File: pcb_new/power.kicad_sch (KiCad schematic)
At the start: 36 parts, among them J2 632723300011, J3 SACC-DSIV-M12MS-5CON-L180, U11 TPS2023DR, U12 LM1085ISX-3.3/NOPB, U13 INA226AIDGSR

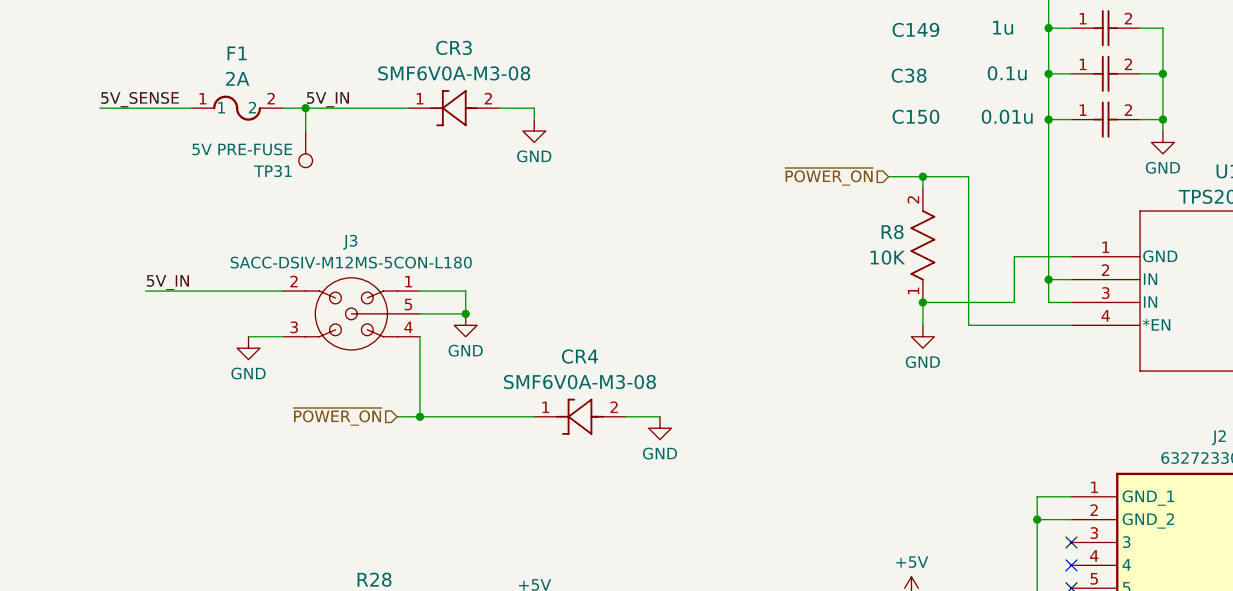
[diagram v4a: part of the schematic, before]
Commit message: separate VBUS/PSU control lines (ref #89) and pull up VBUS enable (ref #68)
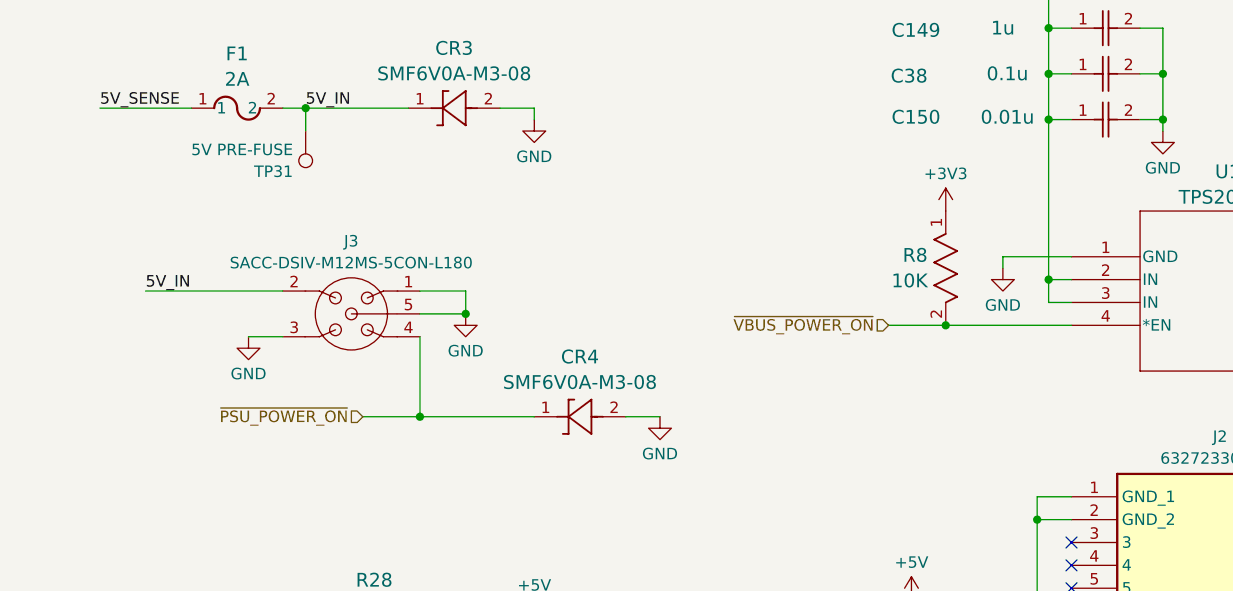
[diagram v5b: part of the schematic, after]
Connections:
- net +3V3: now also R8.1
- net GND: no longer R8.1
- net ~{POWER_ON} renamed ~{PSU_POWER_ON}
- net ~{PSU_POWER_ON}: no longer R8.2, U11.4 (*EN)
- new net ~{VBUS_POWER_ON}: R8.2, U11.4 (*EN)
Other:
- moved on the sheet: R8
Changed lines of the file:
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@@
 	)
 	(junction
-		(at 190.5 57.15)
+		(at 107.95 163.83)
 		(diameter 0)
 		(color 0 0 0 0)
 	)
 	(junction
-		(at 107.95 163.83)
+		(at 193.04 59.69)
 		(diameter 0)
 		(color 0 0 0 0)
@@
 	)
 	(junction
-		(at 190.5 43.18)
-		(diameter 0)
-		(color 0 0 0 0)
-	)
-	(junction
 		(at 129.54 124.46)
 		(diameter 0)
@@
 	(wire
 		(pts
-			(xy 132.08 69.85) (xy 134.62 69.85)
+			(xy 128.27 69.85) (xy 134.62 69.85)
 		)
 		(stroke
@@
 	(wire
 		(pts
-			(xy 195.58 59.69) (xy 207.01 59.69)
-		)
-		(stroke
-			(width 0)
-			(type default)
-		)
-	)
-	(wire
-		(pts
 			(xy 129.54 124.46) (xy 130.81 124.46)
 		)
@@
 	(wire
 		(pts
-			(xy 186.69 43.18) (xy 190.5 43.18)
+			(xy 186.69 59.69) (xy 193.04 59.69)
 		)
 		(stroke
@@
 	(wire
 		(pts
-			(xy 107.95 158.75) (xy 107.95 163.83)
+			(xy 193.04 59.69) (xy 207.01 59.69)
 		)
 		(stroke
@@
 	(wire
 		(pts
-			(xy 49.53 173.99) (xy 49.53 176.53)
+			(xy 107.95 158.75) (xy 107.95 163.83)
 		)
 		(stroke
@@
 	(wire
 		(pts
-			(xy 104.14 111.76) (xy 115.57 111.76)
+			(xy 49.53 173.99) (xy 49.53 176.53)
 		)
 		(stroke
@@
 	(wire
 		(pts
-			(xy 38.1 114.3) (xy 43.18 114.3)
+			(xy 104.14 111.76) (xy 115.57 111.76)
 		)
 		(stroke
@@
 	(wire
 		(pts
-			(xy 195.58 43.18) (xy 195.58 59.69)
+			(xy 38.1 114.3) (xy 43.18 114.3)
 		)
 		(stroke
@@
 	(wire
 		(pts
-			(xy 200.66 57.15) (xy 190.5 57.15)
-		)
-		(stroke
-			(width 0)
-			(type default)
-		)
-	)
-	(wire
-		(pts
 			(xy 129.54 119.38) (xy 129.54 124.46)
 		)
@@
 	(wire
 		(pts
-			(xy 190.5 44.45) (xy 190.5 43.18)
-		)
-		(stroke
-			(width 0)
-			(type default)
-		)
-	)
-	(wire
-		(pts
 			(xy 256.54 27.94) (xy 255.27 27.94)
 		)
@@
 	(wire
 		(pts
-			(xy 190.5 59.69) (xy 190.5 57.15)
-		)
-		(stroke
-			(width 0)
-			(type default)
-		)
-	)
-	(wire
-		(pts
 			(xy 246.38 52.07) (xy 259.08 52.07)
 		)
@@
 	(wire
 		(pts
-			(xy 190.5 43.18) (xy 195.58 43.18)
-		)
-		(stroke
-			(width 0)
-			(type default)
-		)
-	)
-	(wire
-		(pts
 			(xy 204.47 36.83) (xy 204.47 54.61)
 		)
@@
 	(wire
 		(pts
-			(xy 207.01 52.07) (xy 200.66 52.07)
+			(xy 207.01 52.07) (xy 199.39 52.07)
 		)
 		(stroke
@@
 	(wire
 		(pts
-			(xy 200.66 52.07) (xy 200.66 57.15)
+			(xy 255.27 143.51) (xy 243.84 143.51)
 		)
 		(stroke
@@
 	(wire
 		(pts
-			(xy 255.27 143.51) (xy 243.84 143.51)
+			(xy 214.63 31.75) (xy 217.17 31.75)
 		)
 		(stroke
@@
 	(wire
 		(pts
-			(xy 214.63 31.75) (xy 217.17 31.75)
+			(xy 243.84 140.97) (xy 255.27 140.97)
 		)
 		(stroke
@@
 	(wire
 		(pts
-			(xy 243.84 140.97) (xy 255.27 140.97)
+			(xy 199.39 52.07) (xy 199.39 53.34)
 		)
 		(stroke
@@
 		)
 	)
-	(hierarchical_label "~{POWER_ON}"
+	(hierarchical_label "~{PSU_POWER_ON}"
 		(shape input)
-		(at 132.08 69.85 180)
+		(at 128.27 69.85 180)
 		(fields_autoplaced yes)
 		(effects
@@
 		)
 	)
-	(hierarchical_label "~{POWER_ON}"
+	(hierarchical_label "~{VBUS_POWER_ON}"
 		(shape input)
-		(at 186.69 43.18 180)
+		(at 186.69 59.69 180)
 		(fields_autoplaced yes)
 		(effects
@@
 	)
 	(symbol
+		(lib_id "power:+3V3")
+		(at 193.04 46.99 0)
+		(unit 1)
+		(exclude_from_sim no)
+		(in_bom yes)
+		(on_board yes)
+		(dnp no)
+		(fields_autoplaced yes)
+		(property "Reference" "#PWR0198"
+			(at 193.04 50.8 0)
+			(effects
+				(font
+					(size 1.27 1.27)
+				)
+				(hide yes)
+			)
+		)
+		(property "Value" "+3V3"
+			(at 193.04 42.8569 0)
+			(effects
+				(font
+					(size 1.27 1.27)
+				)
+			)
+		)
+		(property "Footprint" ""
+			(at 193.04 46.99 0)
+			(effects
+				(font
+					(size 1.27 1.27)
+				)
+				(hide yes)
+			)
+		)
+		(property "Datasheet" ""
+			(at 193.04 46.99 0)
+			(effects
+				(font
+					(size 1.27 1.27)
+				)
+				(hide yes)
+			)
+		)
+		(property "Description" "Power symbol creates a global label with name \"+3V3\""
+			(at 193.04 46.99 0)
+			(effects
+				(font
+					(size 1.27 1.27)
+				)
+				(hide yes)
+			)
+		)
+		(pin "1"
+		)
+		(instances
+			(project "link"
+				(path "/b8dafc19-6de0-4c8f-9903-23372e5103df/efe900f0-e311-40d9-a69c-d0ffa18ab615"
+					(reference "#PWR0198")
+					(unit 1)
+				)
+			)
+		)
+	)
+	(symbol
 		(lib_id "OroLink:RMCF0402FT10K0")
 		(at 265.43 45.72 90)
@@
 	(symbol
 		(lib_id "OroLink:RMCF0402FT10K0")
-		(at 190.5 57.15 90)
+		(at 193.04 46.99 90)
+		(mirror x)
 		(unit 1)
 		(exclude_from_sim no)
@@
 		(on_board yes)
 		(dnp no)
-		(fields_autoplaced yes)
 		(property "Reference" "R8"
-			(at 188.4934 49.3835 90)
+			(at 191.0334 51.9235 90)
 			(effects
 				(font
@@
 		)
 		(property "Value" "10K"
-			(at 188.4934 52.2164 90)
+			(at 191.0334 54.7564 90)
 			(effects
 				(font
@@
 		)
 		(property "Footprint" "OroLink:STA_RMCF0402_STP"
-			(at 190.5 57.15 0)
+			(at 193.04 46.99 0)
 			(effects
 				(font
@@
 		)
 		(property "Datasheet" "https://www.mouser.de/datasheet/2/385/SEI_RMCF_RMCP-3077565.pdf"
-			(at 190.5 57.15 0)
+			(at 193.04 46.99 0)
 			(effects
 				(font
@@
 		)
 		(property "Description" "Res Thick Film 0402 10K Ohm 1% 0.063W ±100ppm/°C Molded SMD Paper T/R"
-			(at 190.5 57.15 0)
+			(at 193.04 46.99 0)
 			(effects
 				(font
@@
 		)
 		(property "Description_1" "Res Thick Film 0402 10K Ohm 1% 0.063W ±100ppm/°C Molded SMD Paper T/R"
-			(at 193.5 57.15 0)
+			(at 196.04 46.99 0)
 			(effects
 				(font
@@
 		)
 		(property "Mfr. Name" "Stackpole International"
-			(at 193.5 57.15 0)
+			(at 196.04 46.99 0)
 			(effects
 				(font
@@
 		)
 		(property "DigiKey ID" "RMCF0402FT10K0CT-ND"
-			(at 193.5 57.15 0)
+			(at 196.04 46.99 0)
 			(effects
 				(font
@@
 		)
 		(property "Mouser URL" "https://www.mouser.de/ProductDetail/SEI-Stackpole/RMCF0402FT10K0?qs=FESYatJ8odLDpjm%252BwxiA1Q%3D%3D&utm_source=octopart&utm_medium=aggregator&utm_campaign=708-RMCF0402FT10K0&utm_content=SEI%20Stackpole"
-			(at 193.5 57.15 0)
+			(at 196.04 46.99 0)
 			(effects
 				(font
@@
 		)
 		(property "Arrow ID" "RMCF0402FT10K0"
-			(at 193.5 57.15 0)
+			(at 196.04 46.99 0)
 			(effects
 				(font
@@
 		)
 		(property "Mfr. Number" "RMCF0402FT10K0"
-			(at 193.5 57.15 0)
+			(at 196.04 46.99 0)
 			(effects
 				(font
@@
 		)
 		(property "Mouser ID" "708-RMCF0402FT10K0"
-			(at 193.5 57.15 0)
+			(at 196.04 46.99 0)
 			(effects
 				(font
@@
 	(symbol
 		(lib_id "power:GND")
-		(at 190.5 59.69 0)
+		(at 199.39 53.34 0)
 		(unit 1)
 		(exclude_from_sim no)
@@
 		(dnp no)
 		(property "Reference" "#PWR020"
-			(at 190.5 66.04 0)
+			(at 199.39 59.69 0)
 			(effects
 				(font
@@
 		)
 		(property "Value" "GND"
-			(at 190.5 63.8231 0)
+			(at 199.39 57.4731 0)
 			(effects
 				(font
@@
 		)
 		(property "Footprint" ""
-			(at 190.5 59.69 0)
+			(at 199.39 53.34 0)
 			(effects
 				(font
@@
 		)
 		(property "Datasheet" ""
-			(at 190.5 59.69 0)
+			(at 199.39 53.34 0)
 			(effects
 				(font
@@
 		)
 		(property "Description" "Power symbol creates a global label with name \"GND\" , ground"
-			(at 190.5 59.69 0)
+			(at 199.39 53.34 0)
 			(effects
 				(font

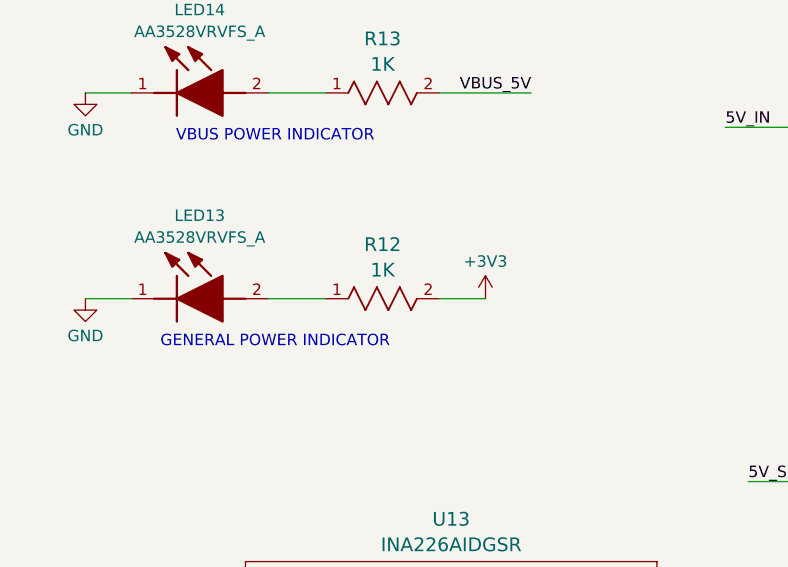
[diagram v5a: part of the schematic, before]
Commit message: reduce general power indicator light intensity
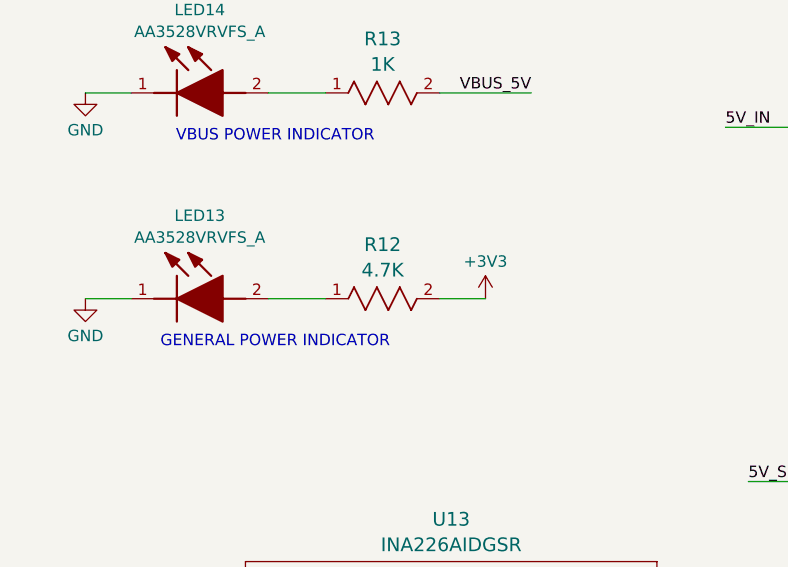
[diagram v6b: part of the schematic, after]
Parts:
- removed R12: 1K, OroLink:RES_SG73P_2A_KOA, symbol OroLink:SG73P2ATTD102J
- added R12: 4.7K, OroLink:RES_CRCW_0402_VIS-L, symbol OroLink:CRCW04024K70FKEDHP
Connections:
- net +3V3: now also R12.2
- net at LED13.2 (A): now also R12.1
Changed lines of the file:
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@@
 	)
 	(symbol
-		(lib_id "OroLink:SG73P2ATTD102J")
-		(at 59.69 74.93 0)
+		(lib_id "OroLink:CRCW04024K70FKEDHP")
+		(at 72.39 74.93 180)
 		(unit 1)
 		(exclude_from_sim no)
@@
 			)
 		)
-		(property "Value" "1K"
+		(property "Value" "4.7K"
 			(at 66.04 71.7609 0)
 			(effects
@@
 			)
 		)
-		(property "Footprint" "OroLink:RES_SG73P_2A_KOA"
-			(at 59.69 74.93 0)
+		(property "Footprint" "OroLink:RES_CRCW_0402_VIS-L"
+			(at 72.39 74.93 0)
 			(effects
 				(font
@@
 			)
 		)
-		(property "Datasheet" "null"
-			(at 59.69 74.93 0)
+		(property "Datasheet" "https://www.vishay.com/doc?20043"
+			(at 72.39 74.93 0)
 			(effects
 				(font
@@
 			)
 		)
-		(property "Description" "Res Thick Film 0805 1K Ohm 5% 0.5W(1/2W) ±100ppm/C Pad SMD Automotive T/R"
-			(at 59.69 74.93 0)
+		(property "Description" "CRCW0402-HP 100 4K7 1% ET7 E3"
+			(at 72.39 74.93 0)
 			(effects
 				(font
@@
 			)
 		)
-		(property "Mouser URL" "null"
-			(at 59.69 77.93 0)
+		(property "Mouser ID" "71-CRCW04024K70FKEDH"
+			(at 72.39 71.93 0)
 			(effects
 				(font
@@
 			)
 		)
-		(property "Arrow ID" "SG73P2ATTD102J"
-			(at 59.69 77.93 0)
+		(property "Mouser URL" "https://www.mouser.de/ProductDetail/Vishay-Dale/CRCW04024K70FKEDHP?qs=k2%2FDWSARqgH3ASlI4vM3KQ%3D%3D&utm_source=octopart&utm_medium=aggregator&utm_campaign=71-CRCW04024K70FKEDH&utm_content=Vishay"
+			(at 72.39 71.93 0)
 			(effects
 				(font
@@
 			)
 		)
-		(property "Mouser ID" "660-SG73P2ATTD102J"
-			(at 59.69 77.93 0)
+		(property "Mfr. Number" "CRCW04024K70FKEDHP"
+			(at 72.39 71.93 0)
 			(effects
 				(font
@@
 			)
 		)
-		(property "Description_1" "Res Thick Film 0805 1K Ohm 5% 0.5W(1/2W) ±100ppm/C Pad SMD Automotive T/R"
-			(at 59.69 77.93 0)
+		(property "DigiKey ID" "541-4.70KYCT-ND"
+			(at 72.39 71.93 0)
 			(effects
 				(font
@@
 			)
 		)
-		(property "DigiKey ID" "2019-SG73P2ATTD102JCT-ND"
-			(at 59.69 77.93 0)
+		(property "Mfr. Name" "Vishay"
+			(at 72.39 71.93 0)
 			(effects
 				(font
@@
 			)
 		)
-		(property "Mfr. Number" "SG73P2ATTD102J"
-			(at 59.69 77.93 0)
+		(property "Description_1" "CRCW0402-HP 100 4K7 1% ET7 E3"
+			(at 72.39 71.93 0)
 			(effects
 				(font
@@
 			)
 		)
-		(property "Mfr. Name" "KOA Speer"
-			(at 59.69 77.93 0)
+		(property "Arrow ID" "CRCW04024K70FKEDHP"
+			(at 72.39 71.93 0)
 			(effects
 				(font
@@
 		)
 		(instances
-			(project ""
+			(project "link"
 				(path "/b8dafc19-6de0-4c8f-9903-23372e5103df/efe900f0-e311-40d9-a69c-d0ffa18ab615"
 					(reference "R12")

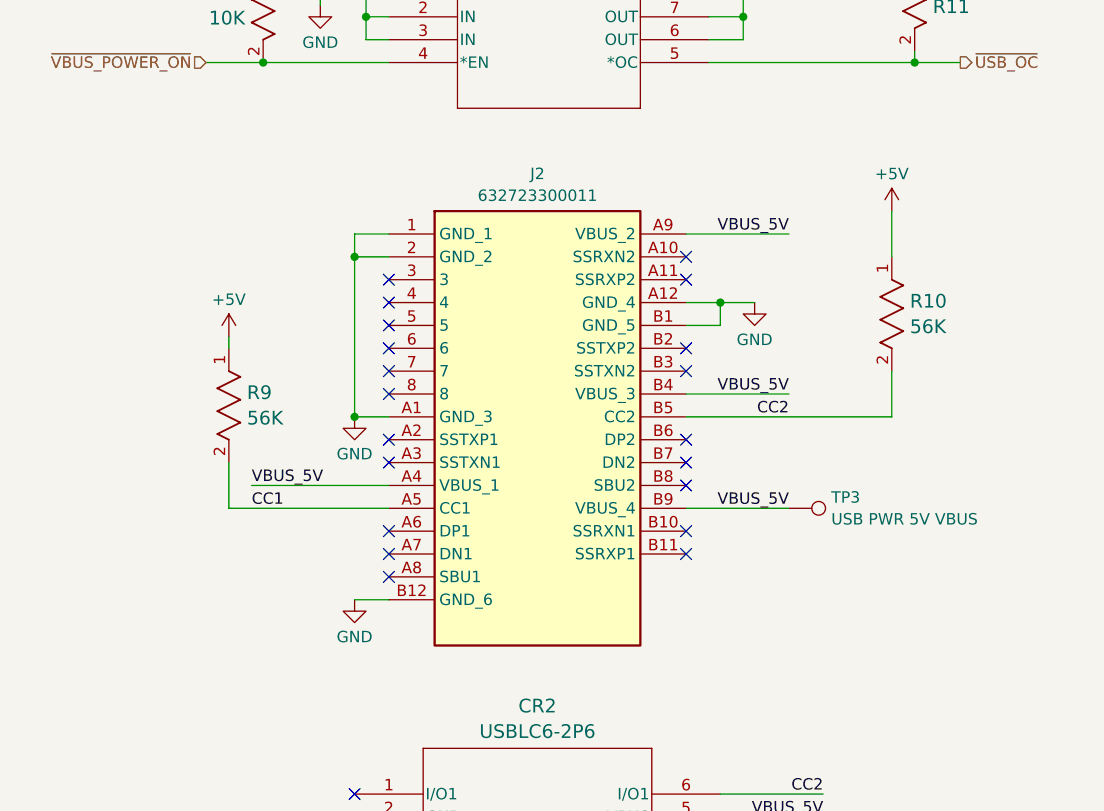
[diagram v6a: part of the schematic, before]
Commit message: replace USB-C receptacle (ref #73)
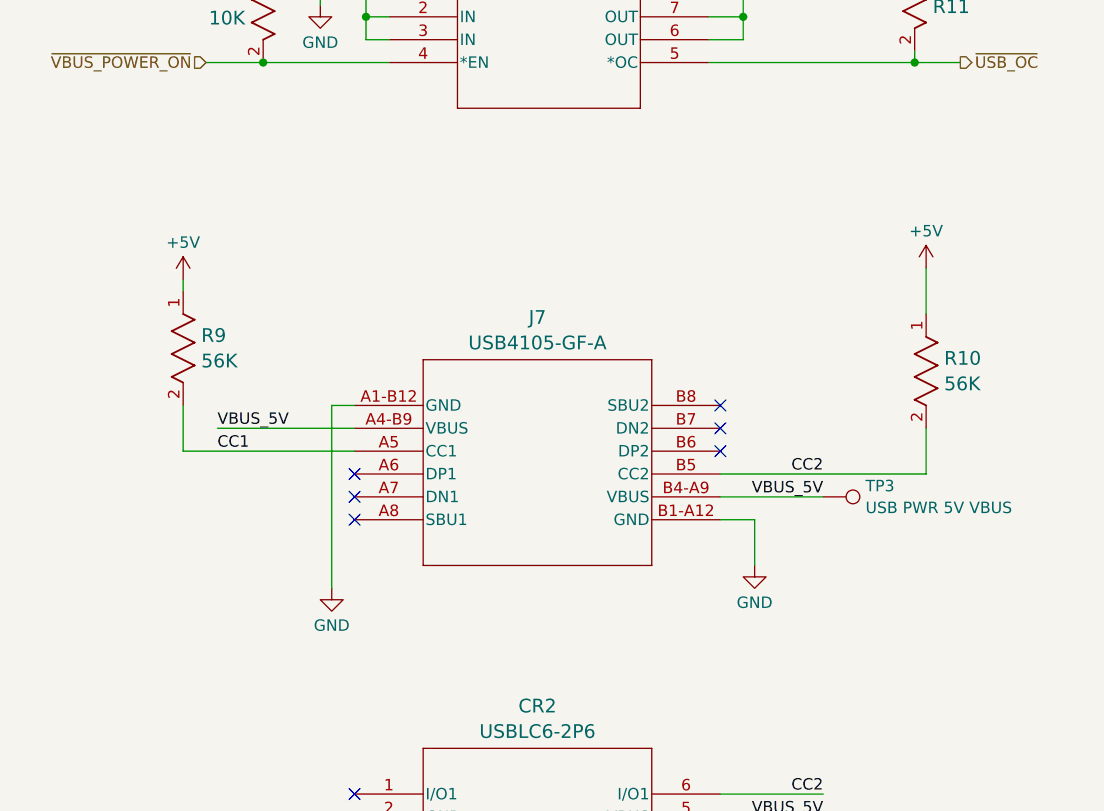
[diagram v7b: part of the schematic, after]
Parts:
- removed J2: 632723300011, OroLink:632723300011, symbol OroLink:632723300011
- added J7: USB4105-GF-A, OroLink:USB4105_GCT, symbol OroLink:USB4105-GF-A
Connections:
- net CC1: now also J7.A5 (CC1)
- net CC2: now also J7.B5 (CC2)
- net GND: now also J7.A1-B12 (GND), J7.B1-A12 (GND)
- net VBUS_5V: now also J7.A4-B9 (VBUS), J7.B4-A9 (VBUS)
- no-connect marks 22 -> 8
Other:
- moved on the sheet: R10, R9, TP3
